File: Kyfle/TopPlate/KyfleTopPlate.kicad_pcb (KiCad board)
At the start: 2 copper layers, 164 x 146.3 mm, 38 parts, among them SW2 KEY_SWITCH, SW2 PRO MICRO

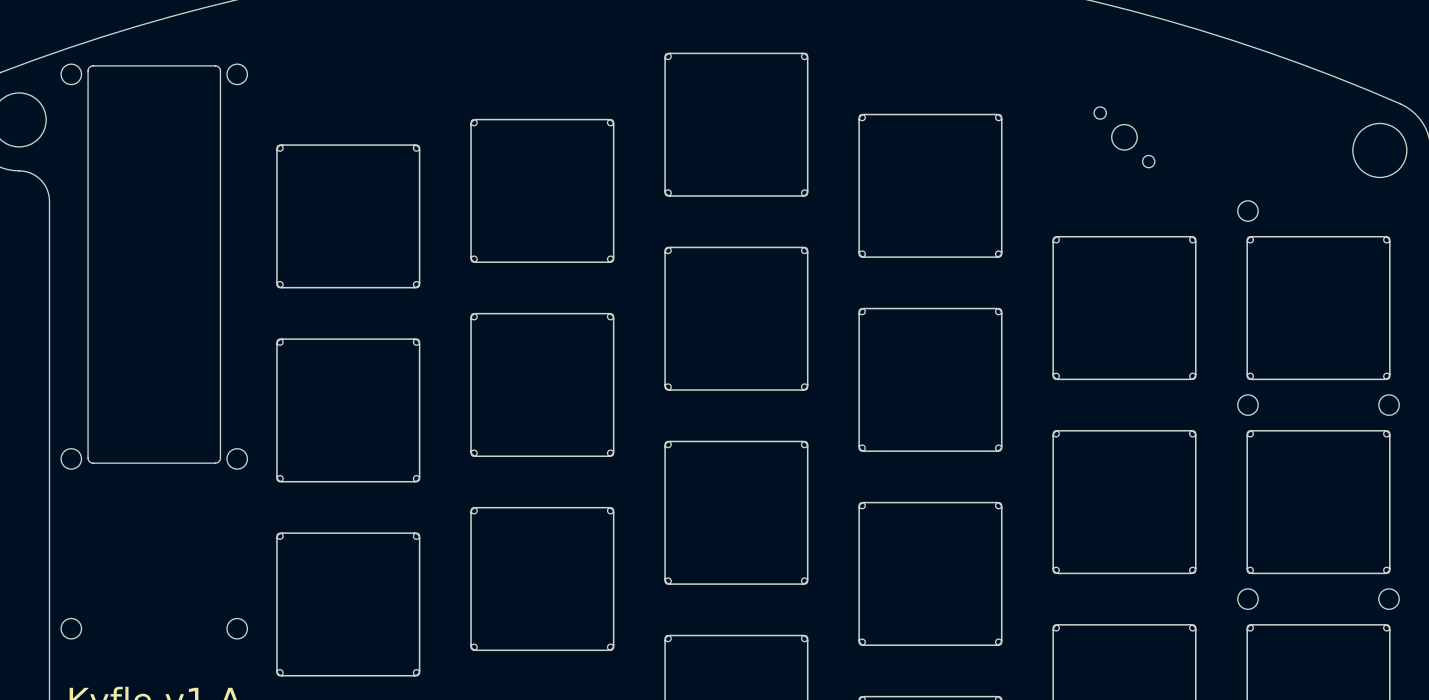
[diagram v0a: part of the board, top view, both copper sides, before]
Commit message: Plates: Received M2 and M5 hardware. It's bigger than specified...
- M5 screw head is ~9.5 instead of 8.7. Was colliding in the top left 
corner with M2 screw for pro micro board. So I shifted up pro micro 
board 0.3mm.
- M2 screw head is also larger than expected (3.8 instead of 3.2). But 
it is mostly fine as I was designing with 4-4.2mm clearance. Only 
exception was for screws supporting the middle bottom section of top 
plate with rails. Here it was colliding with switch housing. So, only 
solution is to use so called reduced slotted screws (DIN 920) as they 
have 2.8mm diameter head.
- Also added JLCPCB silk reference
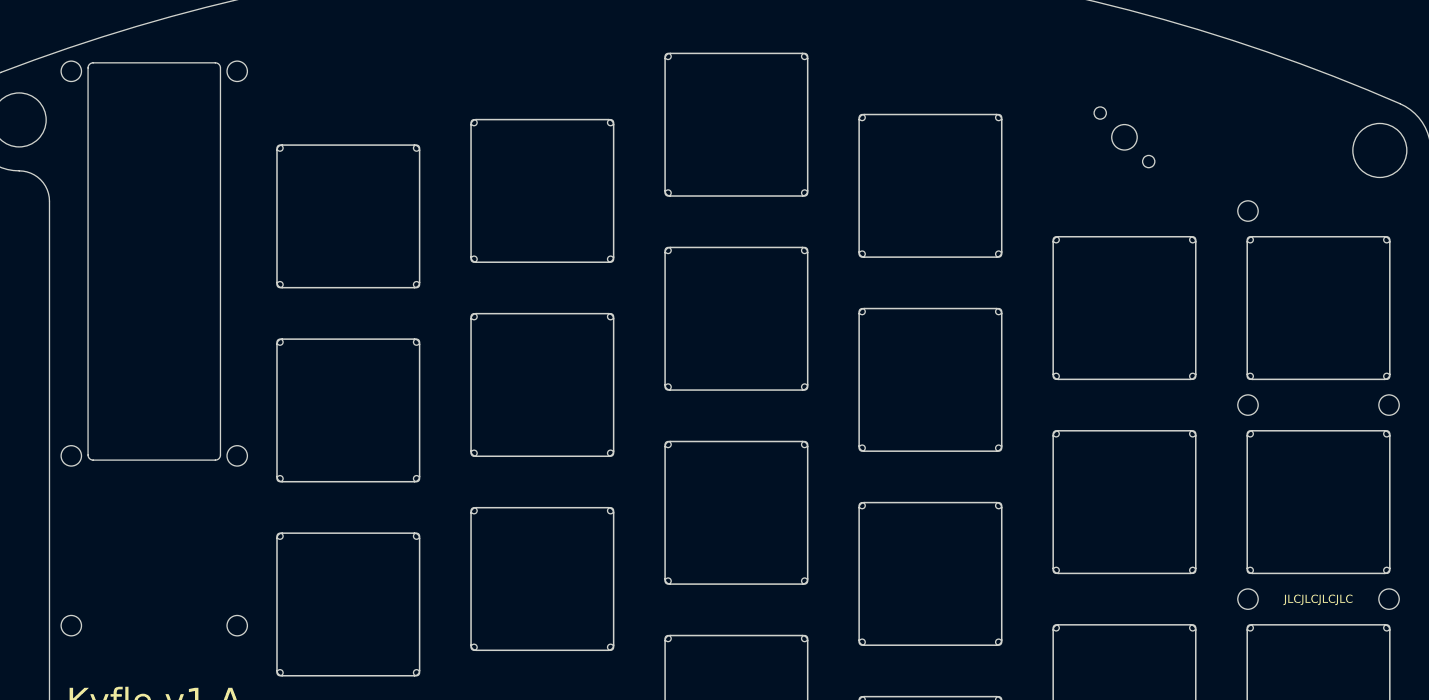
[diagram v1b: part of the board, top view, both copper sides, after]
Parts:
- added JLCJLCJLCJLC: JLCBCB_OrderNumber, Kyfle Footprints:JLCBCB_OrderNumber, F.Cu at (226.2, 82.0)
- moved SW2 0.30 mm to (111.9, 58.4)
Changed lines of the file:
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@@
-(kicad_pcb (version 20171130) (host pcbnew 5.1.11-e4df9d881f~92~ubuntu20.04.1)
+(kicad_pcb (version 20171130) (host pcbnew 5.1.10-88a1d61d58~88~ubuntu18.04.1)
   (general
     (thickness 1.6)
@@
     (tracks 0)
     (zones 0)
-    (modules 38)
+    (modules 39)
     (nets 1)
   )
@@
     (pad_to_mask_clearance 0)
     (aux_axis_origin 0 0)
-    (grid_origin 226.2 53.4)
+    (grid_origin 226.2 91.5)
     (visible_elements 7FFFFF7F)
     (pcbplotparams
@@
     (uvia_drill 0.1)
   )
+  (module "Kyfle Footprints:M5_with_washer_and_board" (layer F.Cu)
+    (at 237.220381 136.74)
+    (descr "Mounting Hole 2.2mm, no annular, M2, ISO14580")
+    (tags "mounting hole 2.2mm no annular m2 iso14580")
+    (attr virtual)
+    (fp_text reference REF** (at 0 -5.25) (layer F.SilkS) hide
+      (effects (font (size 1 1) (thickness 0.15)))
+    )
+    (fp_text value MountingHole_2.2mm_M2_ISO14580 (at 0 5.25) (layer F.Fab) hide
+      (effects (font (size 1 1) (thickness 0.15)))
+    )
+    (fp_circle (center -5 0) (end 0 0) (layer F.CrtYd) (width 0.05))
+    (fp_arc (start 5 0) (end 5 -5) (angle -90) (layer Eco2.User) (width 0.12))
+    (fp_arc (start -15 0) (end -10 0) (angle -90) (layer Eco2.User) (width 0.12))
+    (fp_arc (start -5 0) (end -10 0) (angle -180) (layer Eco2.User) (width 0.12))
+    (fp_text user %R (at 0.3 0) (layer F.Fab) hide
+      (effects (font (size 1 1) (thickness 0.15)))
+    )
+    (pad "" np_thru_hole circle (at -5 0) (size 5.3 5.3) (drill 5.3) (layers *.Cu *.Mask)
+      (clearance 2.35))
+  )
+  (module "Kyfle Footprints:M5_with_washer_and_board" (layer F.Cu)
+    (at 102.174433 163.064671 315)
+    (descr "Mounting Hole 2.2mm, no annular, M2, ISO14580")
+    (tags "mounting hole 2.2mm no annular m2 iso14580")
+    (attr virtual)
+    (fp_text reference REF** (at 0 -5.250001 135) (layer F.SilkS) hide
+      (effects (font (size 1 1) (thickness 0.15)))
+    )
+    (fp_text value MountingHole_2.2mm_M2_ISO14580 (at 0 5.250001 135) (layer F.Fab) hide
+      (effects (font (size 1 1) (thickness 0.15)))
+    )
+    (fp_circle (center -5 0) (end 0 0) (layer F.CrtYd) (width 0.05))
+    (fp_arc (start 5 0) (end 5 -5) (angle -90) (layer Eco2.User) (width 0.12))
+    (fp_arc (start -15 0) (end -10 0) (angle -90) (layer Eco2.User) (width 0.12))
+    (fp_arc (start -5 0) (end -10 0) (angle -180) (layer Eco2.User) (width 0.12))
+    (fp_text user %R (at 0.3 0 135) (layer F.Fab) hide
+      (effects (font (size 1 1) (thickness 0.15)))
+    )
+    (pad "" np_thru_hole circle (at -5 0 315) (size 5.3 5.3) (drill 5.3) (layers *.Cu *.Mask)
+      (clearance 2.35))
+  )
+  (module "Kyfle Footprints:M5_with_washer" (layer F.Cu)
+    (at 98.638899 34.932171 90)
+    (descr "Mounting Hole 2.2mm, no annular, M2, ISO14580")
+    (tags "mounting hole 2.2mm no annular m2 iso14580")
+    (attr virtual)
+    (fp_text reference REF** (at 0 -5.25 90) (layer F.SilkS) hide
+      (effects (font (size 1 1) (thickness 0.15)))
+    )
+    (fp_text value MountingHole_2.2mm_M2_ISO14580 (at 0 5.25 90) (layer F.Fab) hide
+      (effects (font (size 1 1) (thickness 0.15)))
+    )
+    (fp_circle (center 0 0) (end 5 0) (layer F.CrtYd) (width 0.05))
+    (fp_text user %R (at 0.3 0 90) (layer F.Fab) hide
+      (effects (font (size 1 1) (thickness 0.15)))
+    )
+    (pad "" np_thru_hole circle (at 0 0 90) (size 5.3 5.3) (drill 5.3) (layers *.Cu *.Mask)
+      (clearance 2.35))
+  )
+  (module "Kyfle Footprints:M5_with_washer" (layer F.Cu)
+    (at 232.220381 37.928844)
+    (descr "Mounting Hole 2.2mm, no annular, M2, ISO14580")
+    (tags "mounting hole 2.2mm no annular m2 iso14580")
+    (attr virtual)
+    (fp_text reference REF** (at 0 -5.25) (layer F.SilkS) hide
+      (effects (font (size 1 1) (thickness 0.15)))
+    )
+    (fp_text value MountingHole_2.2mm_M2_ISO14580 (at 0 5.25) (layer F.Fab) hide
+      (effects (font (size 1 1) (thickness 0.15)))
+    )
+    (fp_circle (center 0 0) (end 5 0) (layer F.CrtYd) (width 0.05))
+    (fp_text user %R (at 0.3 0) (layer F.Fab) hide
+      (effects (font (size 1 1) (thickness 0.15)))
+    )
+    (pad "" np_thru_hole circle (at 0 0) (size 5.3 5.3) (drill 5.3) (layers *.Cu *.Mask)
+      (clearance 2.35))
+  )
+  (module "Kyfle Footprints:JLCBCB_OrderNumber" (layer F.Cu)
+    (at 226.2 81.975 180)
+    (fp_text reference JLCJLCJLCJLC (at 0 0) (layer F.SilkS)
+      (effects (font (size 0.8 0.8) (thickness 0.15)))
+    )
+    (fp_text value JLCBCB_OrderNumber (at 0 -0.5) (layer F.Fab)
+      (effects (font (size 1 1) (thickness 0.15)))
+    )
+    (fp_line (start -4.5 1) (end -4.5 -1) (layer F.CrtYd) (width 0.12))
+    (fp_line (start 4.5 1) (end -4.5 1) (layer F.CrtYd) (width 0.12))
+    (fp_line (start 4.5 -1) (end 4.5 1) (layer F.CrtYd) (width 0.12))
+    (fp_line (start -4.5 -1) (end 4.5 -1) (layer F.CrtYd) (width 0.12))
+  )
   (module "Kyfle Footprints:SK6812_Bit_Bottom" (layer F.Cu)
     (at 207.15 36.6375)
@@
   )
   (module "Kyfle Footprints:Arduino_ProMicro_Kyfle_v1_TopPlate" (layer F.Cu)
-    (at 111.9 58.6875)
+    (at 111.9 58.3875)
     (fp_text reference SW2 (at 7 -10.95) (layer F.SilkS) hide
       (effects (font (size 1 1) (thickness 0.15)))
@@
       (clearance 1.1))
   )
-  (module "Kyfle Footprints:M5_with_washer_and_board" (layer F.Cu)
-    (at 237.220381 136.74)
-    (descr "Mounting Hole 2.2mm, no annular, M2, ISO14580")
-    (tags "mounting hole 2.2mm no annular m2 iso14580")
-    (attr virtual)
-    (fp_text reference REF** (at 0 -5.25) (layer F.SilkS) hide
-      (effects (font (size 1 1) (thickness 0.15)))
-    )
-    (fp_text value MountingHole_2.2mm_M2_ISO14580 (at 0 5.25) (layer F.Fab) hide
-      (effects (font (size 1 1) (thickness 0.15)))
-    )
-    (fp_circle (center -5 0) (end -0.6 0) (layer F.CrtYd) (width 0.05))
-    (fp_arc (start 5 0) (end 5 -5) (angle -90) (layer Eco2.User) (width 0.12))
-    (fp_arc (start -15 0) (end -10 0) (angle -90) (layer Eco2.User) (width 0.12))
-    (fp_arc (start -5 0) (end -10 0) (angle -180) (layer Eco2.User) (width 0.12))
-    (fp_text user %R (at 0.3 0) (layer F.Fab) hide
-      (effects (font (size 1 1) (thickness 0.15)))
-    )
-    (pad "" np_thru_hole circle (at -5 0) (size 5.3 5.3) (drill 5.3) (layers *.Cu *.Mask)
-      (clearance 1.85))
-  )
-  (module "Kyfle Footprints:M5_with_washer_and_board" (layer F.Cu)
-    (at 102.174433 163.064671 315)
-    (descr "Mounting Hole 2.2mm, no annular, M2, ISO14580")
-    (tags "mounting hole 2.2mm no annular m2 iso14580")
-    (attr virtual)
-    (fp_text reference REF** (at 0 -5.250001 135) (layer F.SilkS) hide
-      (effects (font (size 1 1) (thickness 0.15)))
-    )
-    (fp_text value MountingHole_2.2mm_M2_ISO14580 (at 0 5.250001 135) (layer F.Fab) hide
-      (effects (font (size 1 1) (thickness 0.15)))
-    )
-    (fp_circle (center -5 0) (end -0.6 0) (layer F.CrtYd) (width 0.05))
-    (fp_arc (start 5 0) (end 5 -5) (angle -90) (layer Eco2.User) (width 0.12))
-    (fp_arc (start -15 0) (end -10 0) (angle -90) (layer Eco2.User) (width 0.12))
-    (fp_arc (start -5 0) (end -10 0) (angle -180) (layer Eco2.User) (width 0.12))
-    (fp_text user %R (at 0.3 0 135) (layer F.Fab) hide
-      (effects (font (size 1 1) (thickness 0.15)))
-    )
-    (pad "" np_thru_hole circle (at -5 0 315) (size 5.3 5.3) (drill 5.3) (layers *.Cu *.Mask)
-      (clearance 1.85))
-  )
-  (module "Kyfle Footprints:M5_with_washer" (layer F.Cu)
-    (at 98.638899 34.932171 90)
-    (descr "Mounting Hole 2.2mm, no annular, M2, ISO14580")
-    (tags "mounting hole 2.2mm no annular m2 iso14580")
-    (attr virtual)
-    (fp_text reference REF** (at 0 -5.25 90) (layer F.SilkS) hide
-      (effects (font (size 1 1) (thickness 0.15)))
-    )
-    (fp_text value MountingHole_2.2mm_M2_ISO14580 (at 0 5.25 90) (layer F.Fab) hide
-      (effects (font (size 1 1) (thickness 0.15)))
-    )
-    (fp_circle (center 0 0) (end 4.4 0) (layer F.CrtYd) (width 0.05))
-    (fp_text user %R (at 0.3 0 90) (layer F.Fab) hide
-      (effects (font (size 1 1) (thickness 0.15)))
-    )
-    (pad "" np_thru_hole circle (at 0 0 90) (size 5.3 5.3) (drill 5.3) (layers *.Cu *.Mask)
-      (clearance 1.85))
-  )
-  (module "Kyfle Footprints:M5_with_washer" (layer F.Cu)
-    (at 232.220381 37.928844)
-    (descr "Mounting Hole 2.2mm, no annular, M2, ISO14580")
-    (tags "mounting hole 2.2mm no annular m2 iso14580")
-    (attr virtual)
-    (fp_text reference REF** (at 0 -5.25) (layer F.SilkS) hide
-      (effects (font (size 1 1) (thickness 0.15)))
-    )
-    (fp_text value MountingHole_2.2mm_M2_ISO14580 (at 0 5.25) (layer F.Fab) hide
-      (effects (font (size 1 1) (thickness 0.15)))
-    )
-    (fp_circle (center 0 0) (end 4.4 0) (layer F.CrtYd) (width 0.05))
-    (fp_text user %R (at 0.3 0) (layer F.Fab) hide
-      (effects (font (size 1 1) (thickness 0.15)))
-    )
-    (pad "" np_thru_hole circle (at 0 0) (size 5.3 5.3) (drill 5.3) (layers *.Cu *.Mask)
-      (clearance 1.85))
-  )
   (module "Kyfle Footprints:M2_with_washer" (layer F.Cu)
     (at 169.05 104.05 90)
@@
       )
     )
+  )
+  (zone (net 0) (net_name "") (layers F&B.Cu) (hatch edge 0.508)
+    (connect_pads (clearance 0.2))
+    (min_thickness 0.254)
+    (keepout (tracks not_allowed) (vias not_allowed) (copperpour not_allowed))
+    (fill (arc_segments 32) (thermal_gap 0.508) (thermal_bridge_width 0.508))
+    (polygon
+      (pts
+        (xy 102.4 31.1) (xy 98.8 31.1) (xy 98.8 28.5) (xy 102.4 28.5)
+      )
+    )

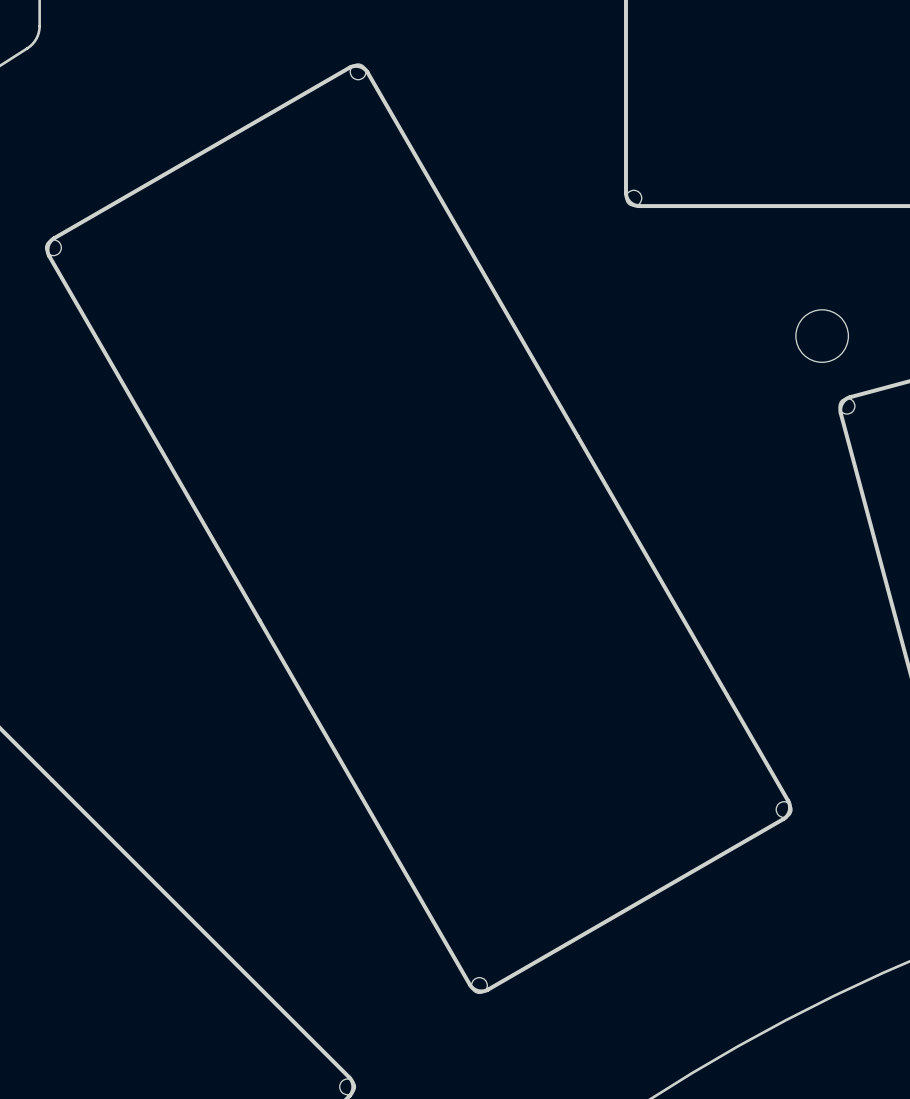
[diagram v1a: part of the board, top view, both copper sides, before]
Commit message: Adds mouse bites to top plate with rails
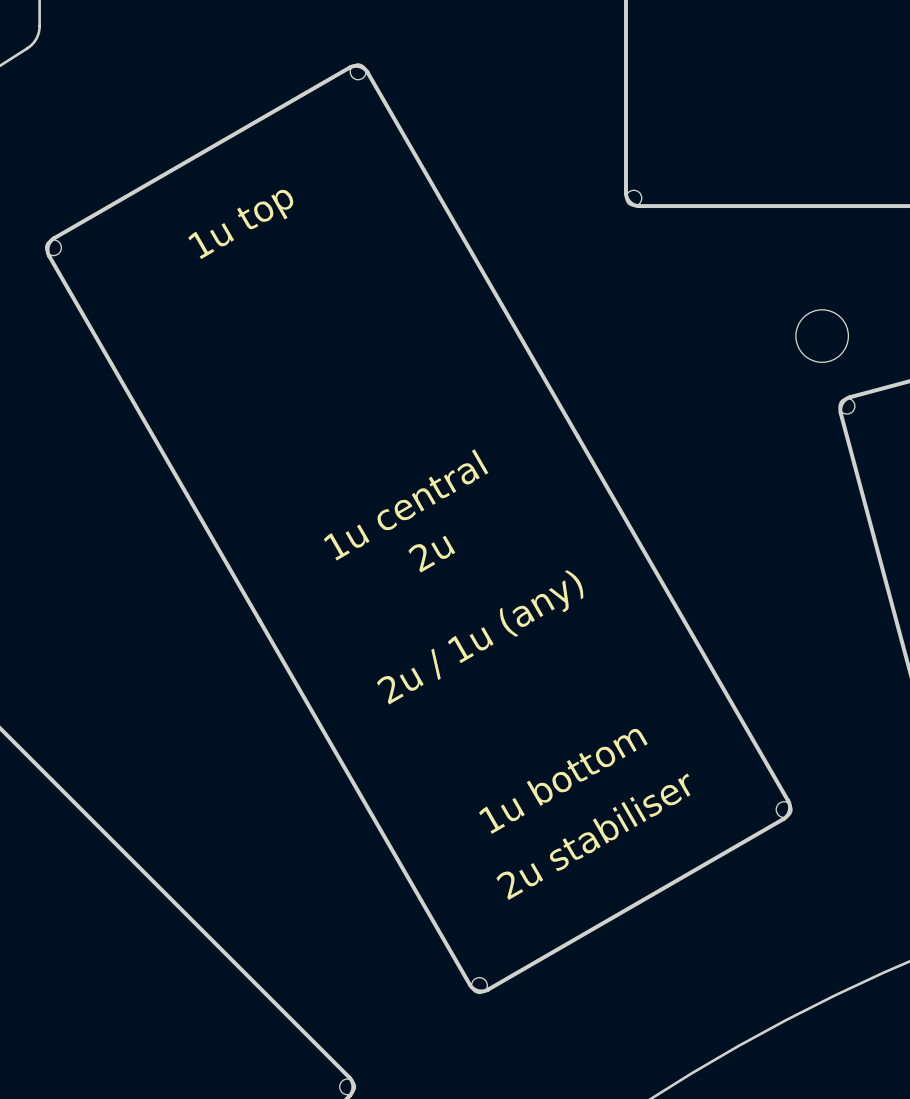
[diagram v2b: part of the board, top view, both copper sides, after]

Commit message: First attempts at supporting Pimoroni trackball
Will be further refined once I can take real measurements on them
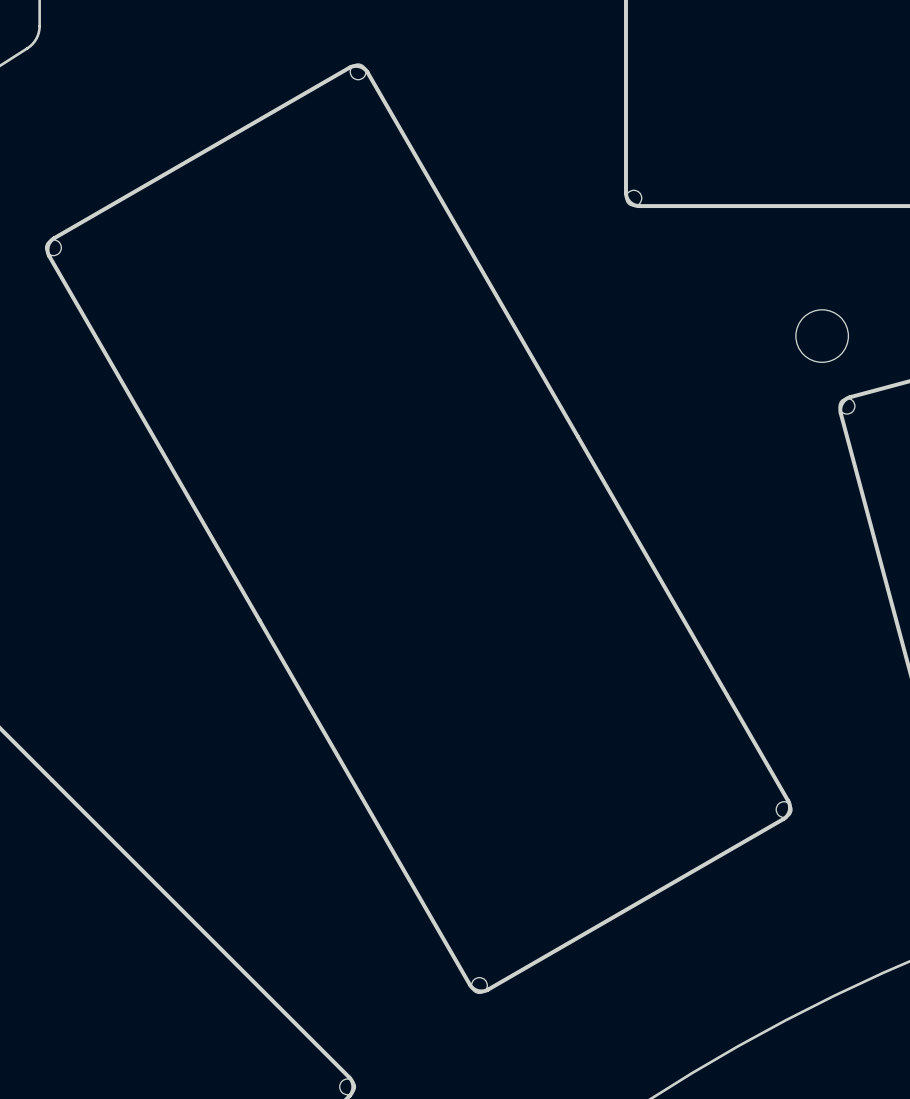
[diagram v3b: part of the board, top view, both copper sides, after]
